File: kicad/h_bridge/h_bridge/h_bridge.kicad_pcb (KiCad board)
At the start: 2 copper layers, 59 parts, among them J1 Conn_01x04_Male, J2 voltage_in, J3 motor, Q1 IRF3205, Q2 IRF3205, Q3 IRF3205, Q4 IRF3205, Q5 IRF3205, Q6 IRF3205, Q7 IRF3205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

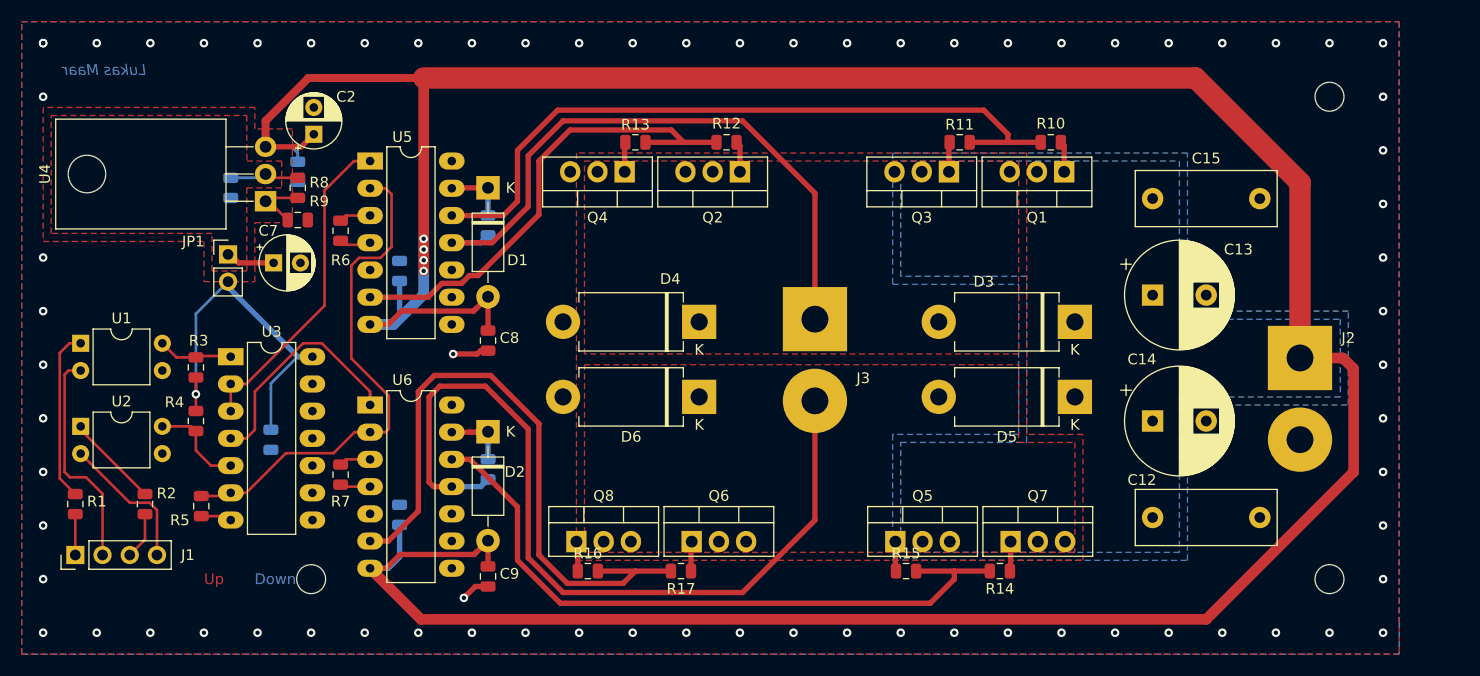
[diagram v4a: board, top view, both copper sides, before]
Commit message: [kicad/h_bridge] outlines added
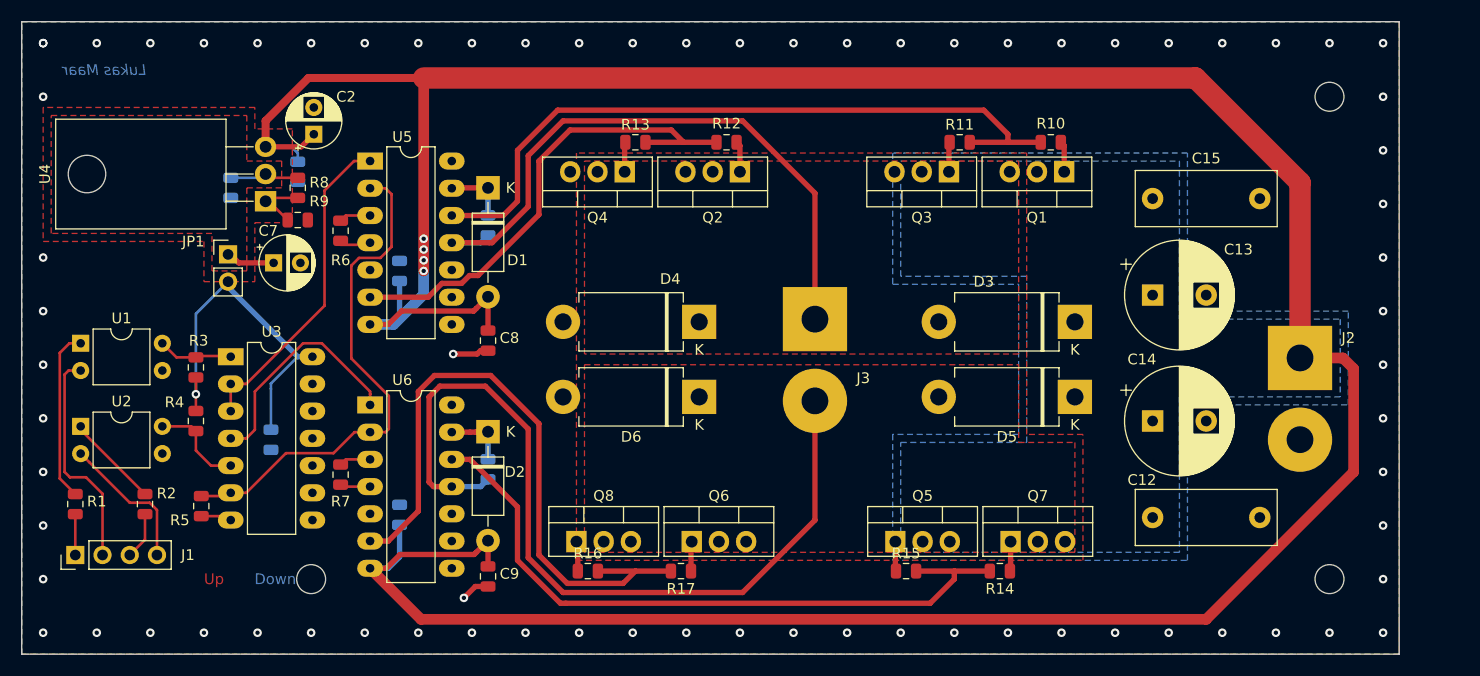
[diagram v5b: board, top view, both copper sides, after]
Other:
- board outline added: 128.5 x 59 mm
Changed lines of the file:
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@@
   (general
     (thickness 1.6)
-    (drawings 3)
+    (drawings 7)
     (tracks 311)
     (zones 0)
@@
     (visible_elements FFFFFF7F)
     (pcbplotparams
-      (layerselection 0x010fc_ffffffff)
+      (layerselection 0x0d0fc_ffffffff)
       (usegerberextensions false)
       (usegerberattributes false)
@@
     )
   )
+  (gr_line (start 229 98) (end 100.5 98) (layer Edge.Cuts) (width 0.05))
+  (gr_line (start 229 157) (end 229 98) (layer Edge.Cuts) (width 0.05))
+  (gr_line (start 100.5 157) (end 229 157) (layer Edge.Cuts) (width 0.05))
+  (gr_line (start 100.5 98) (end 100.5 157) (layer Edge.Cuts) (width 0.05))
   (gr_text "Lukas Maar" (at 108.25 102.5) (layer B.Cu)
     (effects (font (size 1 1) (thickness 0.15) italic) (justify mirror))
